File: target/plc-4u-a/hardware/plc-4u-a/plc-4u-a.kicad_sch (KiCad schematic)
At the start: 103 parts, among them J1 Screw_Terminal_01x02, J10 AUX_INS, J11 X Leds Btns, J13 Valve control in, J14 Leak sensors, J15 I2C, J19 Valve leds, J2 Screw_Terminal_01x02, J3 Screw_Terminal_01x02, J4 Screw_Terminal_01x02, J5 Screw_Terminal_01x02, J52 U8 IN, J53 X0, J55 AVR-ISP-10, J58 U17 OUT, J59 U8 OUT, J6 V_ST_HWS, J61 GND, J63 VCC, J69 VDD, J7 V_ST_CWS, J79 NC, J8 W_CT_HWS, J81 NC, J83 RXD, J85 TXD, J9 W_CT_CWS, Q1 IRF4905, Q2 IRF4905, Q3 IRF4905, Q4 IRF4905, Q5 IRF4905, Q6 IRF4905, U1 ATmega16-16P, U10 PC817, U11 PC817, U12 PC817, U13 PC817, U14 PC817, U15 PC817, U16 PC817, U2 PC817, U22 MAX485E, U3 PC817, U4 PC817, U5 PC817, U6 PC817, U7 PC817, U9 PC817, Y1 Crystal

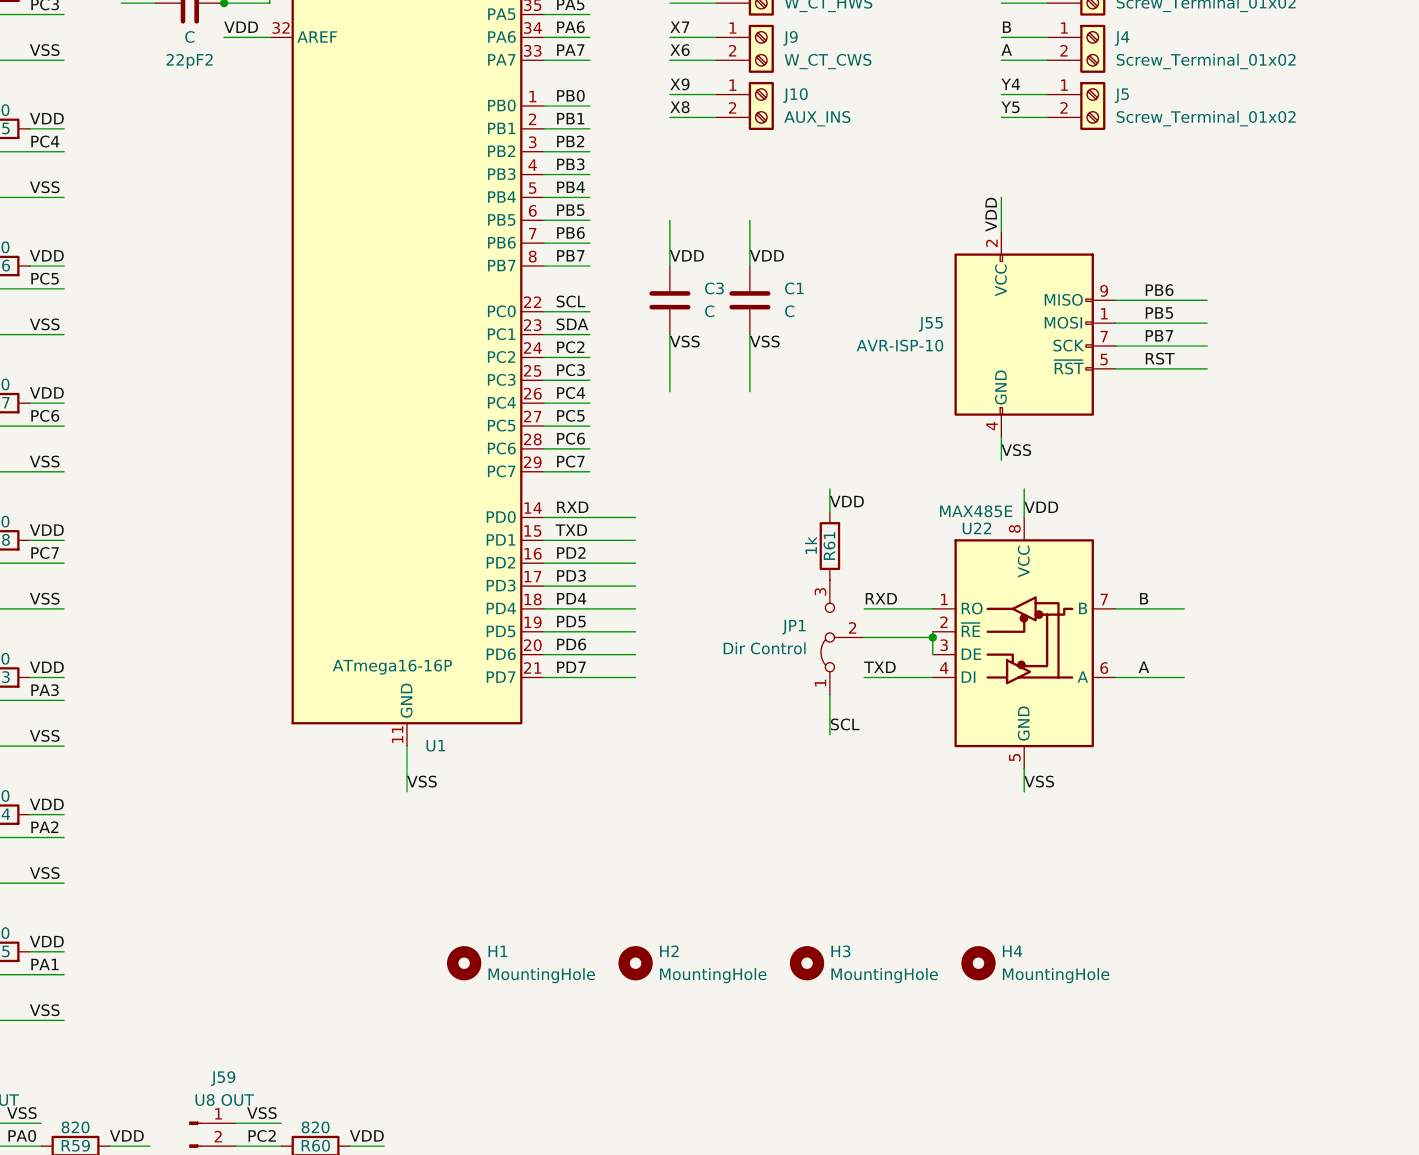
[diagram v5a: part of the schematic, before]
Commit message: plc-4u-a board += RS485 protection
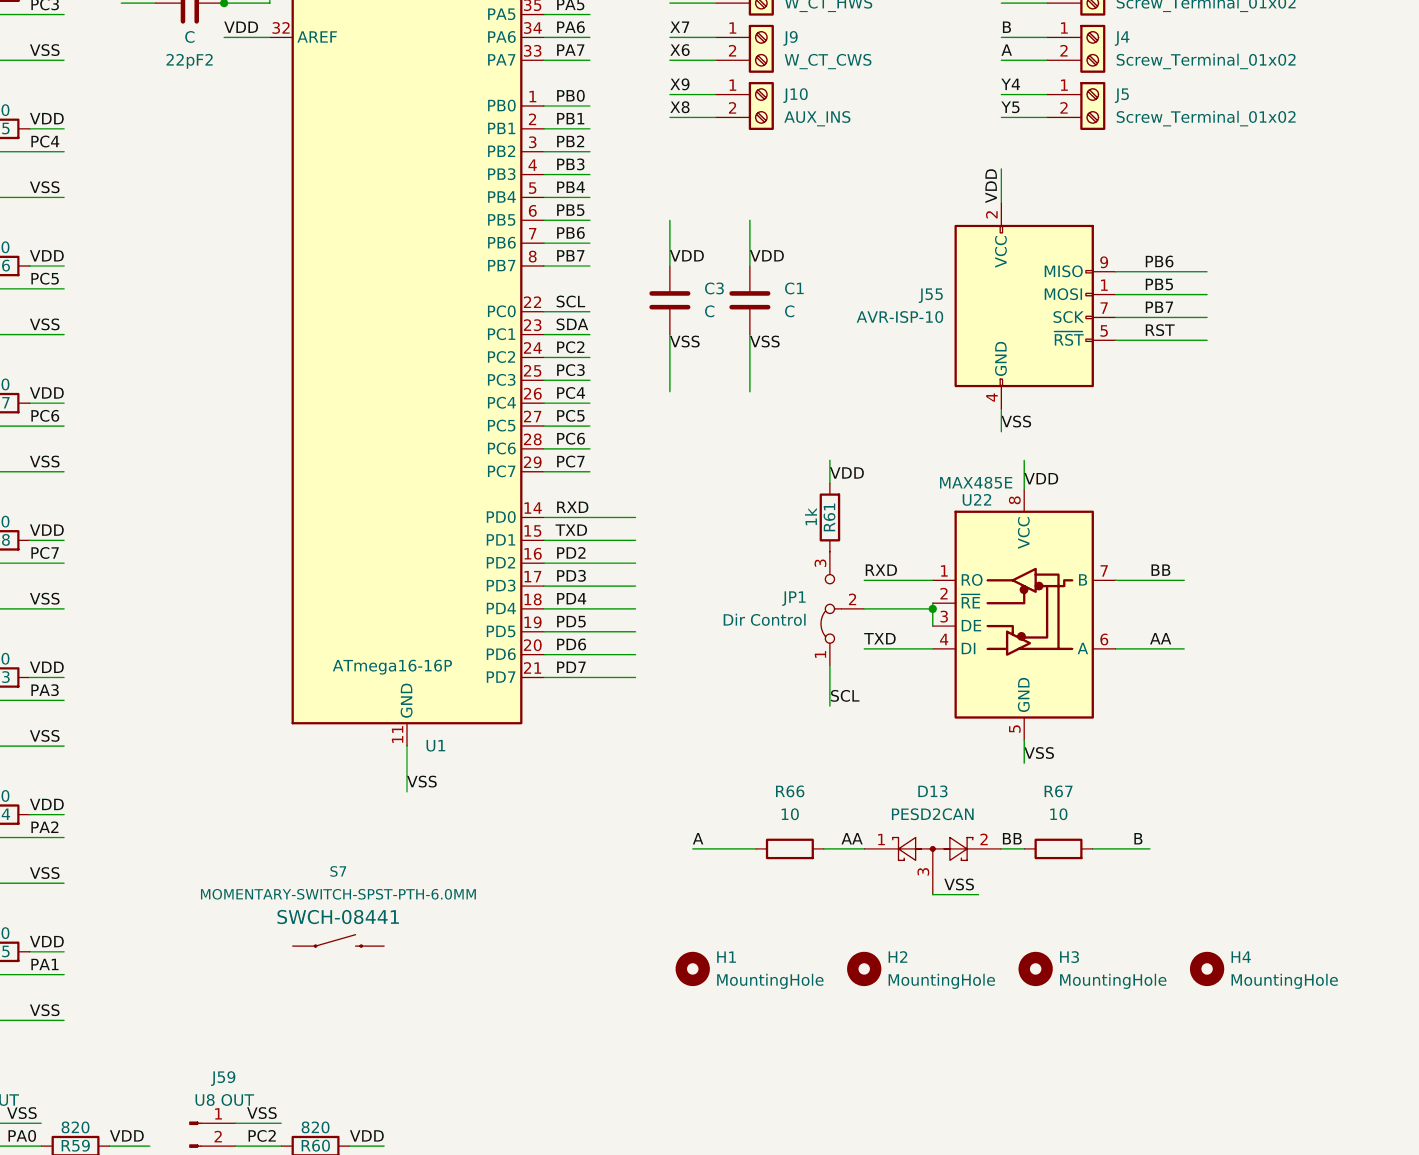
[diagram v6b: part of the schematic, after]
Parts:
- added D13: PESD2CAN, Package_TO_SOT_SMD:SOT-23, symbol Diode:BAT54A
- added R66, R67: 10, Resistor_SMD:R_1206_3216Metric, symbol Device:R
- added S7: MOMENTARY-SWITCH-SPST-PTH-6.0MM, Button_Switch_THT:SW_Tactile_SKHH_Angled, symbol SparkFun-Switches:MOMENTARY-SWITCH-SPST-PTH-6.0MM
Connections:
- net A: now also R66.1; no longer U22.6 (A)
- net B: now also R67.2; no longer U22.7 (B)
- net VSS: now also D13.3
- new net AA: D13.1, R66.2, U22.6 (A)
- new net BB: D13.2, R67.1, U22.7 (B)
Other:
- moved on the sheet: H1, H2, H3, H4, J55, JP1, R61, U22

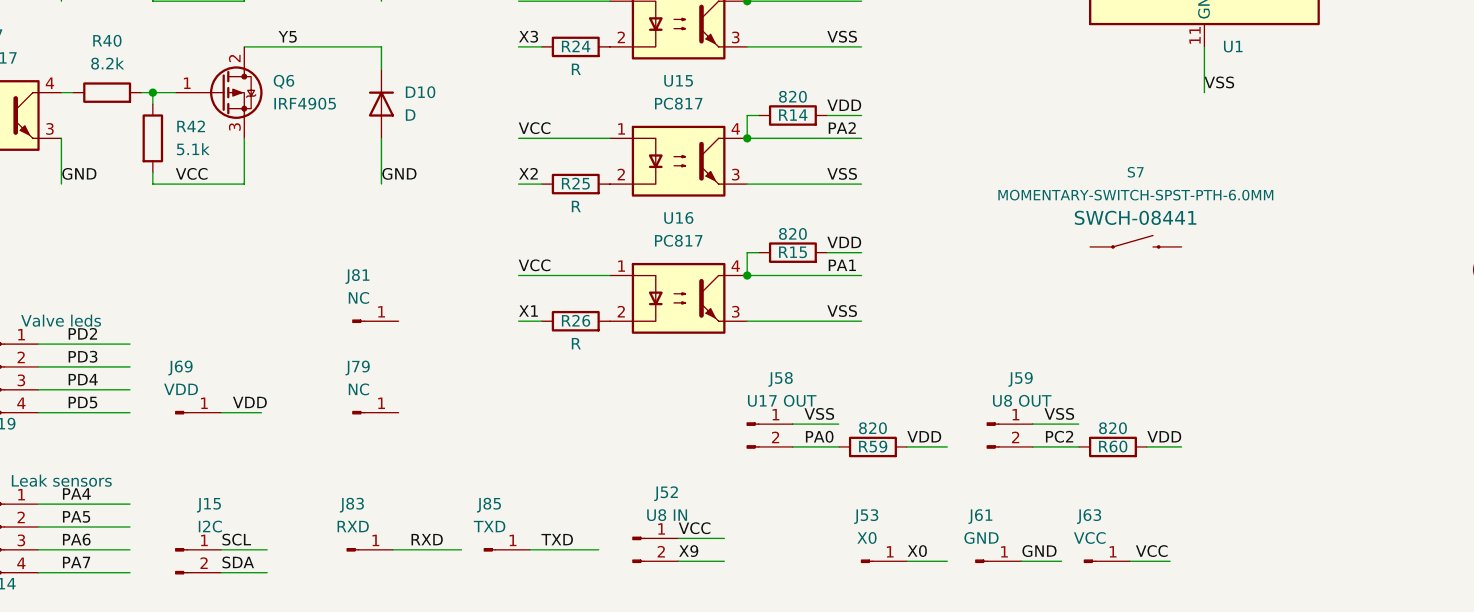
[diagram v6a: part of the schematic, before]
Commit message: plc4u-a: main-retained-register (preparing for buzzer)
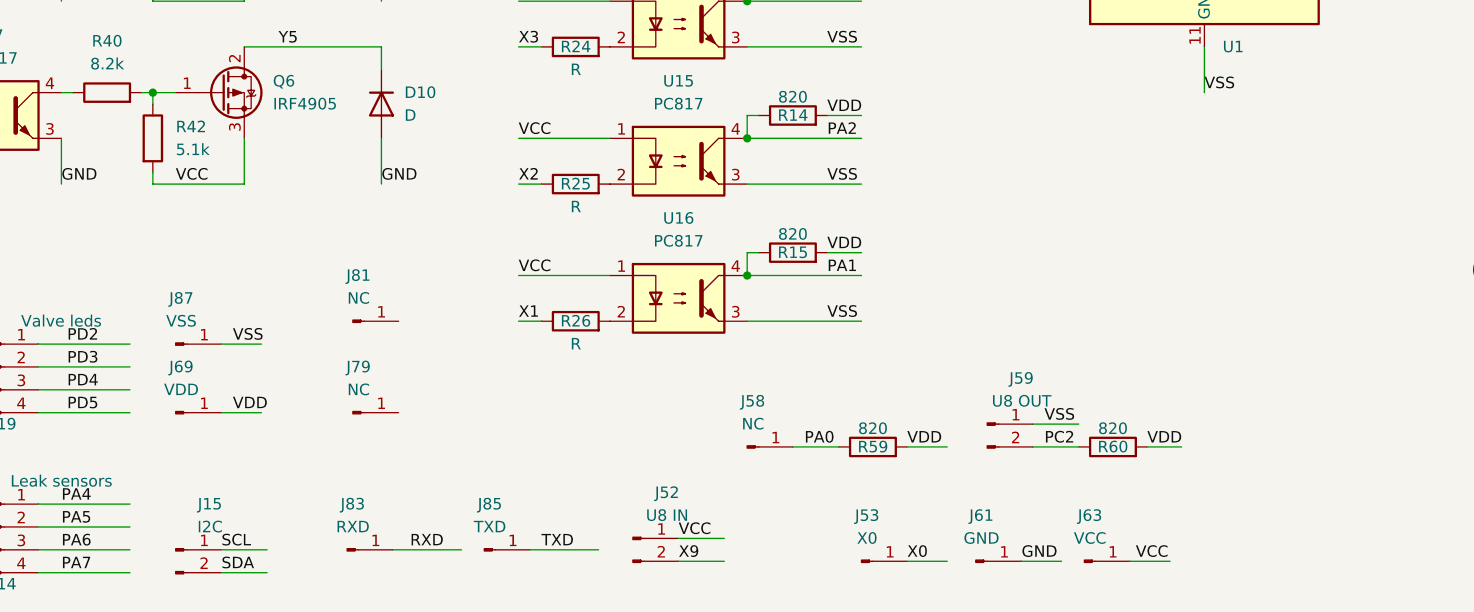
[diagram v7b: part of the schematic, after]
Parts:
- removed J58: U17 OUT, Connector_PinHeader_2.54mm:PinHeader_1x02_P2.54mm_Vertical, symbol Connector:Conn_01x02_Male
- removed S7: MOMENTARY-SWITCH-SPST-PTH-6.0MM, Button_Switch_THT:SW_Tactile_SKHH_Angled, symbol SparkFun-Switches:MOMENTARY-SWITCH-SPST-PTH-6.0MM
- added J58: NC, Connector_PinHeader_2.54mm:PinHeader_1x01_P2.54mm_Vertical, symbol Connector:Conn_01x01_Male
- added J87: VSS, Connector_PinHeader_2.54mm:PinHeader_1x01_P2.54mm_Vertical, symbol Connector:Conn_01x01_Male
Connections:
- net PA0: now also J58.1 (Pin_1)
- net VSS: now also J87.1 (Pin_1)
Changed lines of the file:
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@@
     (stroke (width 0) (type default) (color 0 0 0 0))
   )
+  (wire (pts (xy 68.58 167.64) (xy 73.025 167.64))
+    (stroke (width 0) (type default) (color 0 0 0 0))
+  )
   (wire (pts (xy 33.02 43.18) (xy 35.56 43.18))
     (stroke (width 0) (type default) (color 0 0 0 0))
@@
     (stroke (width 0) (type default) (color 0 0 0 0))
   )
-  (wire (pts (xy 132.08 176.53) (xy 137.16 176.53))
-    (stroke (width 0) (type default) (color 0 0 0 0))
-  )
   (wire (pts (xy 101.6 104.14) (xy 104.14 104.14))
     (stroke (width 0) (type default) (color 0 0 0 0))
@@
     (effects (font (size 1.27 1.27)) (justify left bottom))
   )
-  (label "VSS" (at 133.35 176.53 0)
-    (effects (font (size 1.27 1.27)) (justify left bottom))
-  )
   (label "PA2" (at 194.31 45.72 0)
     (effects (font (size 1.27 1.27)) (justify left bottom))
@@
     (effects (font (size 1.27 1.27)) (justify left bottom))
   )
+  (label "VSS" (at 69.85 167.64 0)
+    (effects (font (size 1.27 1.27)) (justify left bottom))
+  )
   (label "PB2" (at 33.02 190.5 0)
     (effects (font (size 1.27 1.27)) (justify left bottom))
@@
     (pin "4")
   )
+  (symbol (lib_id "Connector:Conn_01x01_Male") (at 63.5 167.64 0) (unit 1)
+    (in_bom yes) (on_board yes) (fields_autoplaced)
+    (property "Reference" "J87" (id 0) (at 64.135 162.56 0))
+    (property "Value" "VSS" (id 1) (at 64.135 165.1 0))
+    (property "Footprint" "Connector_PinHeader_2.54mm:PinHeader_1x01_P2.54mm_Vertical" (id 2) (at 63.5 167.64 0)
+      (effects (font (size 1.27 1.27)) hide)
+    )
+    (property "Datasheet" "~" (id 3) (at 63.5 167.64 0)
+      (effects (font (size 1.27 1.27)) hide)
+    )
+    (pin "1")
+  )
   (symbol (lib_id "Connector:Conn_01x01_Male") (at 83.185 165.1 0) (unit 1)
     (in_bom yes) (on_board yes) (fields_autoplaced)
@@
     (pin "2")
   )
-  (symbol (lib_id "SparkFun-Switches:MOMENTARY-SWITCH-SPST-PTH-6.0MM") (at 170.18 156.845 0) (unit 1)
-    (in_bom yes) (on_board yes) (fields_autoplaced)
-    (property "Reference" "S7" (id 0) (at 170.18 148.59 0)
-      (effects (font (size 1.143 1.143)))
-    )
-    (property "Value" "MOMENTARY-SWITCH-SPST-PTH-6.0MM" (id 1) (at 170.18 151.13 0)
-      (effects (font (size 1.143 1.143)))
-    )
-    (property "Footprint" "Button_Switch_THT:SW_Tactile_SKHH_Angled" (id 2) (at 170.18 151.765 0)
-      (effects (font (size 0.508 0.508)) hide)
-    )
-    (property "Datasheet" "" (id 3) (at 170.18 156.845 0)
-      (effects (font (size 1.27 1.27)) hide)
-    )
-    (property "Field4" " SWCH-08441" (id 4) (at 170.18 153.67 0)
-      (effects (font (size 1.524 1.524)))
-    )
-    (pin "1")
-    (pin "3")
-  )
   (symbol (lib_id "Device:R") (at 107.95 73.66 90) (unit 1)
     (in_bom yes) (on_board yes)
@@
     (pin "2")
   )
-  (symbol (lib_id "Connector:Conn_01x02_Male") (at 127 176.53 0) (unit 1)
-    (in_bom yes) (on_board yes)
-    (property "Reference" "J58" (id 0) (at 130.81 171.45 0))
-    (property "Value" "U17 OUT" (id 1) (at 130.81 173.99 0))
-    (property "Footprint" "Connector_PinHeader_2.54mm:PinHeader_1x02_P2.54mm_Vertical" (id 2) (at 127 176.53 0)
+  (symbol (lib_id "Connector:Conn_01x01_Male") (at 127 179.07 0) (unit 1)
+    (in_bom yes) (on_board yes) (fields_autoplaced)
+    (property "Reference" "J58" (id 0) (at 127.635 173.99 0))
+    (property "Value" "NC" (id 1) (at 127.635 176.53 0))
+    (property "Footprint" "Connector_PinHeader_2.54mm:PinHeader_1x01_P2.54mm_Vertical" (id 2) (at 127 179.07 0)
       (effects (font (size 1.27 1.27)) hide)
     )
-    (property "Datasheet" "~" (id 3) (at 127 176.53 0)
+    (property "Datasheet" "~" (id 3) (at 127 179.07 0)
       (effects (font (size 1.27 1.27)) hide)
     )
     (pin "1")
-    (pin "2")
   )
   (symbol (lib_id "Mechanical:MountingHole") (at 266.7 159.385 0) (unit 1)
@@
       (reference "J55") (unit 1) (value "AVR-ISP-10") (footprint "Connector_IDC:IDC-Header_2x05_P2.54mm_Vertical")
     )
-    (path "/f726a4d4-7c47-433b-b351-06d46a93f59c/a3a69169-58a6-40bf-8176-e6ffa11cae21"
-      (reference "J56") (unit 1) (value "U17 OUT") (footprint "Connector_PinHeader_2.54mm:PinHeader_1x02_P2.54mm_Vertical")
+    (path "/f726a4d4-7c47-433b-b351-06d46a93f59c/ecd6a48b-3d22-4707-889f-33a2504358a0"
+      (reference "J56") (unit 1) (value "PA0") (footprint "Connector_PinHeader_2.54mm:PinHeader_1x01_P2.54mm_Vertical")
     )
     (path "/f726a4d4-7c47-433b-b351-06d46a93f59c/268f40de-bf7c-4350-a3f2-a18be0589762"
       (reference "J57") (unit 1) (value "U8 OUT") (footprint "Connector_PinHeader_2.54mm:PinHeader_1x02_P2.54mm_Vertical")
     )
-    (path "/f0717332-4222-43a8-a537-546d56ff8917"
-      (reference "J58") (unit 1) (value "U17 OUT") (footprint "Connector_PinHeader_2.54mm:PinHeader_1x02_P2.54mm_Vertical")
+    (path "/f185ee33-131c-40f5-a89d-68c429e40d54"
+      (reference "J58") (unit 1) (value "NC") (footprint "Connector_PinHeader_2.54mm:PinHeader_1x01_P2.54mm_Vertical")
     )
     (path "/83d9a264-1e0d-47ef-8074-2f404ea8c192"
@@
     )
     (path "/f726a4d4-7c47-433b-b351-06d46a93f59c/cc46d22f-0194-443e-8b07-030c91da4508"
-      (reference "J71") (unit 1) (value "RESERVED_OUT") (footprint "Connector_PinHeader_2.54mm:PinHeader_1x01_P2.54mm_Vertical")
+      (reference "J71") (unit 1) (value "RESERVED_IN") (footprint "Connector_PinHeader_2.54mm:PinHeader_1x01_P2.54mm_Vertical")
     )
     (path "/f726a4d4-7c47-433b-b351-06d46a93f59c/4167f770-6472-48b7-b17d-528fdefd2576"
@@
       (reference "J86") (unit 1) (value "TXD") (footprint "Connector_PinHeader_2.54mm:PinHeader_1x01_P2.54mm_Vertical")
     )
+    (path "/54c1064f-4083-4f6f-8ca7-f1166d2f8820"
+      (reference "J87") (unit 1) (value "VSS") (footprint "Connector_PinHeader_2.54mm:PinHeader_1x01_P2.54mm_Vertical")
+    )
+    (path "/f726a4d4-7c47-433b-b351-06d46a93f59c/7c86ccec-e2ba-4921-9365-756de896b96e"
+      (reference "J88") (unit 1) (value "VSS") (footprint "Connector_PinHeader_2.54mm:PinHeader_1x01_P2.54mm_Vertical")
+    )
     (path "/6c31e26c-d4f0-4a60-a42c-87884dfba4c7"
       (reference "JP1") (unit 1) (value "Dir Control") (footprint "Jumper:SolderJumper-3_P1.3mm_Bridged2Bar12_Pad1.0x1.5mm")
@@
       (reference "S6") (unit 1) (value "MOMENTARY-SWITCH-SPST-LED-PTH-12MM") (footprint "mod:TACTILE_SWITCH_LED_PTH_12MM")
     )
-    (path "/94e68735-e0ca-44a9-a557-e11642a9a0da"
-      (reference "S7") (unit 1) (value "MOMENTARY-SWITCH-SPST-PTH-6.0MM") (footprint "Button_Switch_THT:SW_Tactile_SKHH_Angled")
-    )
     (path "/1bbd118a-a2aa-467a-bead-76efa852d8cb"
